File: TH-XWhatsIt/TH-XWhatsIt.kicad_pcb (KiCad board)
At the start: 2 copper layers, 178 x 115.5 mm, 41 parts, among them J1 COLUMNS, J10 DISPLAYWRITER PLUGBOARD CONNE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, J11 DISPLAYWRITER PLUGBOARD ROWS, J12 EXPANSION HEADER, J2 ROWS, J3 MODEL F PLUGBOARD COLUMNS, J4 MODEL F PLUGBOARD CONNECTOR, J5 MODEL F PLUGBOARD ROWS, J6 BEAMSPRING PLUGBOARD COLUMNS, J7 BEAMSPRING PLUGBOARD CONNECTOR, J8 BEAMSPRING PLUGBOARD ROWS, J9 DISPLAYWRITER PLUGBOARD COLUM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, U1 LM339, U2 MCP4921-EP, U3 74HCT595, U5 74HCT595, U6 LM339, U7 ProMicro, U8 74HCT595

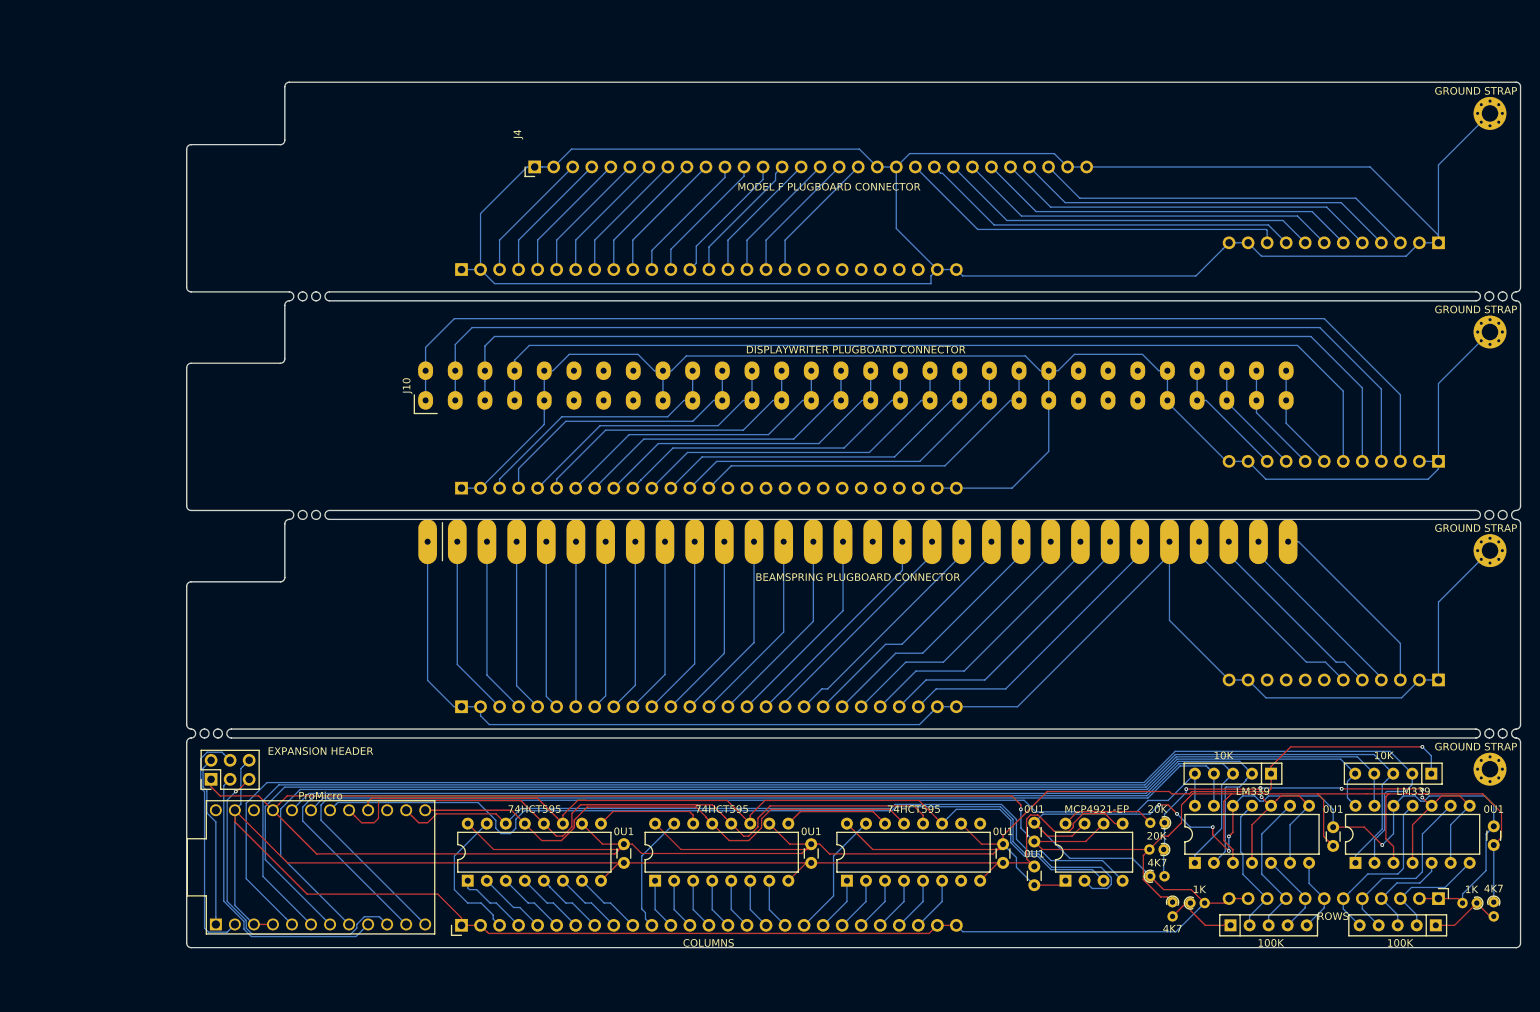
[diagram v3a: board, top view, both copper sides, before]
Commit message: initial update to switch to smd, so now th prefix is a misnomer
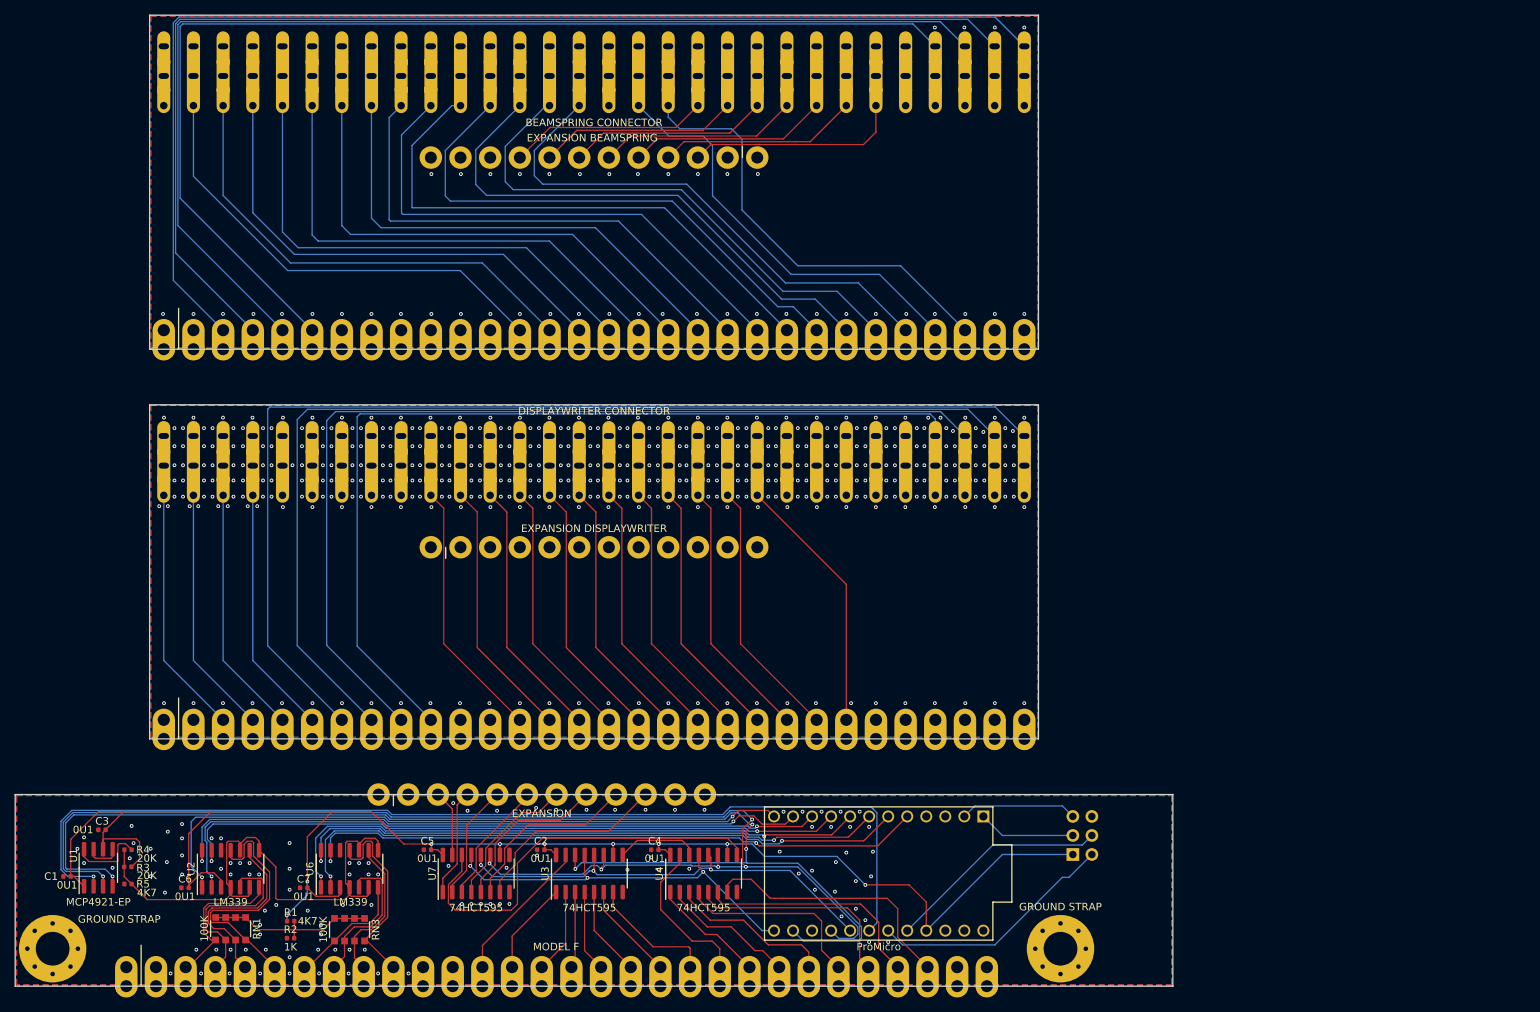
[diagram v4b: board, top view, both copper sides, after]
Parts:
- removed C10, C8, C9: 0U1, Capacitor_THT:C_Disc_D3.0mm_W1.6mm_P2.50mm
- removed H3, H4: GROUND STRAP, MountingHole:MountingHole_2.2mm_M2_Pad_Via
- removed J10: DISPLAYWRITER PLUGBOARD CONNECTOR, TH-XWhatsIt:DIP-60_155_ELL
- removed J11: DISPLAYWRITER PLUGBOARD ROWS, Connector_PinSocket_2.54mm:PinSocket_1x12_P2.54mm_Vertical
- removed J12: EXPANSION HEADER, Connector_PinHeader_2.54mm:PinHeader_2x03_P2.54mm_Vertical
- removed R6: 4K7, Resistor_THT:R_Axial_DIN0204_L3.6mm_D1.6mm_P1.90mm_Vertical
- removed R7: 1K, Resistor_THT:R_Axial_DIN0204_L3.6mm_D1.6mm_P1.90mm_Vertical
- removed RN2, RN4: 10K, Resistor_THT:R_Array_SIP5
- removed U8: 74HCT595, Package_DIP:DIP-16_W7.62mm
- added C1: 0U1, Capacitor_SMD:C_0402_1005Metric, F.Cu at (37.6, 139.3)
- added C2: 0U1, Capacitor_SMD:C_0402_1005Metric, F.Cu at (100.8, 135.8)
- added C6: 0U1, Capacitor_SMD:C_0402_1005Metric, F.Cu at (53.4, 140.8)
- added U4: 74HCT595, Package_SO:SOIC-16_3.9x9.9mm_P1.27mm, F.Cu at (122.6, 138.9)
- C3, C4, C5, C7: footprint Capacitor_THT:C_Disc_D3.0mm_W1.6mm_P2.50mm -> Capacitor_SMD:C_0402_1005Metric
- H1, H2: footprint MountingHole:MountingHole_2.2mm_M2_Pad_Via -> MountingHole:MountingHole_4.5mm_Pad_Via
- J1: value COLUMNS -> MODEL F; footprint Connector_PinHeader_2.54mm:PinHeader_1x27_P2.54mm_Vertical -> TH-XWhatsIt:30-pin-castelated-connector
- J2: value ROWS -> EXPANSION; footprint Connector_PinHeader_2.54mm:PinHeader_1x12_P2.54mm_Vertical -> TH-XWhatsIt:12-pin-castelated-connector
- J3: value MODEL F PLUGBOARD COLUMNS -> EXPANSION HEADER; footprint Connector_PinSocket_2.54mm:PinSocket_1x27_P2.54mm_Vertical -> Connector_PinHeader_2.54mm:PinHeader_2x03_P2.54mm_Horizontal
- J4: value MODEL F PLUGBOARD CONNECTOR -> EXPANSION BEAMSPRING; footprint Connector_PinHeader_2.54mm:PinHeader_1x30_P2.54mm_Horizontal -> TH-XWhatsIt:30-pin-castelated-connector
- J5: value MODEL F PLUGBOARD ROWS -> BEAMSPRING CONNECTOR; footprint Connector_PinSocket_2.54mm:PinSocket_1x12_P2.54mm_Vertical -> TH-XWhatsIt:30-pin-universal-beamspring-connector; moved to F.Cu
- J6: value BEAMSPRING PLUGBOARD COLUMNS -> EXPANSION BEAMSPRING; footprint Connector_PinSocket_2.54mm:PinSocket_1x27_P2.54mm_Vertical -> TH-XWhatsIt:12-pin-castelated-connector; moved to F.Cu
- J7: value BEAMSPRING PLUGBOARD CONNECTOR -> EXPANSION DISPLAYWRITER; footprint TH-XWhatsIt:3..6mm_cardedge -> TH-XWhatsIt:30-pin-castelated-connector
- J8: value BEAMSPRING PLUGBOARD ROWS -> DISPLAYWRITER CONNECTOR; footprint Connector_PinSocket_2.54mm:PinSocket_1x12_P2.54mm_Vertical -> TH-XWhatsIt:30-pin-universal-beamspring-connector; moved to F.Cu
- J9: value DISPLAYWRITER PLUGBOARD COLUMNS -> EXPANSION DISPLAYWRITER; footprint Connector_PinSocket_2.54mm:PinSocket_1x27_P2.54mm_Vertical -> TH-XWhatsIt:12-pin-castelated-connector; moved to F.Cu
- R1, R2, R3, R4, R5: footprint Resistor_THT:R_Axial_DIN0204_L3.6mm_D1.6mm_P1.90mm_Vertical -> Resistor_SMD:R_0402_1005Metric
- RN1, RN3: footprint Resistor_THT:R_Array_SIP5 -> Resistor_SMD:R_Array_Convex_4x1206
- U1: value LM339 -> MCP4921-EP; footprint Package_DIP:DIP-14_W7.62mm -> Package_SO:SOIC-8_3.9x4.9mm_P1.27mm
- U2: value MCP4921-EP -> LM339; footprint Package_DIP:DIP-8_W7.62mm -> Package_SO:SOIC-14_3.9x8.7mm_P1.27mm
- U3: footprint Package_DIP:DIP-16_W7.62mm -> Package_SO:SOIC-16_3.9x9.9mm_P1.27mm
- U5: value 74HCT595 -> ProMicro; footprint Package_DIP:DIP-16_W7.62mm -> promicro:ProMicro
- U6: footprint Package_DIP:DIP-14_W7.62mm -> Package_SO:SOIC-14_3.9x8.7mm_P1.27mm
- U7: value ProMicro -> 74HCT595; footprint promicro:ProMicro -> Package_SO:SOIC-16_3.9x9.9mm_P1.27mm
- moved H1 193.3 mm to (35.7, 149.0)
- moved U1 167.8 mm to (41.8, 138.2)
- moved RN1 160.8 mm to (59.4, 146.3), turned to 270 degrees
- moved R1 160.6 mm to (67.5, 145.3), turned to 0 degrees
- moved R2 158.4 mm to (67.4, 147.6), turned to 0 degrees
- moved R4 138.4 mm to (45.7, 135.8), turned to 0 degrees
- moved R3 138.3 mm to (45.7, 138.0), turned to 0 degrees
- moved R5 136.4 mm to (45.7, 140.3)
- moved H2 125.3 mm to (170.2, 149.0)
- moved C3 124.5 mm to (42.3, 133.1), turned to 0 degrees
- moved J2 120.5 mm to (101.0, 128.4), turned to 0 degrees
- moved RN3 117.6 mm to (75.3, 146.4), turned to 270 degrees
- moved J8 115.8 mm to (107.9, 86.5), turned to 0 degrees
- moved J5 114.5 mm to (107.9, 34.5), turned to 0 degrees
- moved J3 112.9 mm to (171.8, 136.4), turned to 0 degrees
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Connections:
- H2 pad 1: /model f plugboard/MFGROUND -> GNDA
- J1 pad 10: COL8 -> SENSE8
- J1 pad 11: COL9 -> GNDA
- J1 pad 12: COL10 -> GNDA
- J1 pad 13: COL11 -> COL1
- J1 pad 14: COL12 -> COL2
- J1 pad 15: COL13 -> COL3
- J1 pad 16: COL14 -> COL4
- J1 pad 17: COL15 -> COL5
- J1 pad 18: COL16 -> COL6
- J1 pad 19: COL17 -> COL7
- J1 pad 20: COL18 -> COL8
- J1 pad 21: COL19 -> COL9
- J1 pad 22: COL20 -> COL10
- J1 pad 23: COL21 -> COL11
- J1 pad 24: COL22 -> COL12
- J1 pad 25: COL23 -> COL13
- J1 pad 26: GNDA -> COL14
- J1 pad 27: GNDA -> COL15
- J1 pad 3: COL1 -> SENSE1
- J1 pad 4: COL2 -> SENSE2
- J1 pad 5: COL3 -> SENSE3
- J1 pad 6: COL4 -> SENSE4
- J1 pad 7: COL5 -> SENSE5
- J1 pad 8: COL6 -> SENSE7
- J1 pad 9: COL7 -> SENSE6
- J2 pad 10: SENSE8 -> COL24
- J2 pad 3: SENSE1 -> COL17
- J2 pad 4: SENSE2 -> COL18
- J2 pad 5: SENSE3 -> COL19
- J2 pad 6: SENSE4 -> COL20
- J2 pad 7: SENSE5 -> COL21
- J2 pad 8: SENSE7 -> COL22
- J2 pad 9: SENSE6 -> COL23
- J3 pad 1: /model f plugboard/MFGROUND -> +5VA
- J3 pad 2: /model f plugboard/MFGROUND -> HEADER3
- J3 pad 3: /model f plugboard/MFCOL1 -> HEADER1
- J3 pad 4: /model f plugboard/MFCOL2 -> HEADER4
- J3 pad 5: /model f plugboard/MFCOL3 -> HEADER2
- J3 pad 6: /model f plugboard/MFCOL4 -> GNDA
- J4 pad 1: /model f plugboard/MFGROUND -> /beamspring plugboard/BSGROUND
- J4 pad 10: /model f plugboard/MFCOL8 -> Net-(J4-Pad10)
- J4 pad 11: /model f plugboard/MFCOL9 -> /beamspring plugboard/BSGROUND
- J4 pad 12: /model f plugboard/MFCOL10 -> /beamspring plugboard/BSGROUND
- J4 pad 13: /model f plugboard/MFCOL11 -> /beamspring plugboard/BSCOL1
- J4 pad 14: /model f plugboard/MFCOL12 -> /beamspring plugboard/BSCOL2
- J4 pad 15: /model f plugboard/MFCOL13 -> /beamspring plugboard/BSCOL3
- J4 pad 16: /model f plugboard/MFCOL14 -> /beamspring plugboard/BSCOL4
- J4 pad 17: /model f plugboard/MFCOL15 -> /beamspring plugboard/BSCOL5
- J4 pad 18: /model f plugboard/MFCOL16 -> /beamspring plugboard/BSCOL6
- J4 pad 19: /model f plugboard/MFGROUND -> /beamspring plugboard/BSCOL7
- J4 pad 2: /model f plugboard/MFGROUND -> /beamspring plugboard/BSGROUND
- J4 pad 20: /model f plugboard/MFGROUND -> /beamspring plugboard/BSCOL8
- J4 pad 21: /model f plugboard/MFSENSE1 -> /beamspring plugboard/BSCOL9
- J4 pad 22: /model f plugboard/MFSENSE2 -> /beamspring plugboard/BSCOL10
- J4 pad 23: /model f plugboard/MFSENSE3 -> /beamspring plugboard/BSCOL11
- J4 pad 24: /model f plugboard/MFSENSE4 -> /beamspring plugboard/BSCOL12
- J4 pad 25: /model f plugboard/MFSENSE5 -> /beamspring plugboard/BSCOL13
- J4 pad 26: /model f plugboard/MFSENSE6 -> /beamspring plugboard/BSCOL14
- J4 pad 27: /model f plugboard/MFSENSE7 -> /beamspring plugboard/BSCOL15
- J4 pad 28: /model f plugboard/MFSENSE8 -> /beamspring plugboard/BSCOL16
- J4 pad 29: /model f plugboard/MFGROUND -> /beamspring plugboard/BSGROUND
- J4 pad 3: /model f plugboard/MFCOL1 -> /beamspring plugboard/BSSENSE4
- J4 pad 30: /model f plugboard/MFGROUND -> /beamspring plugboard/BSGROUND
- J4 pad 4: /model f plugboard/MFCOL2 -> /beamspring plugboard/BSSENSE3
- J4 pad 5: /model f plugboard/MFCOL3 -> /beamspring plugboard/BSSENSE2
- J4 pad 6: /model f plugboard/MFCOL4 -> /beamspring plugboard/BSSENSE1
- J4 pad 7: /model f plugboard/MFCOL5 -> Net-(J4-Pad7)
- J4 pad 8: /model f plugboard/MFCOL6 -> Net-(J4-Pad8)
- J4 pad 9: /model f plugboard/MFCOL7 -> Net-(J4-Pad9)
- J5 pad 1: /model f plugboard/MFGROUND -> /beamspring plugboard/BSGROUND
- J5 pad 10: /model f plugboard/MFSENSE1 -> /beamspring plugboard/BSCOL9
- J5 pad 11: /model f plugboard/MFGROUND -> /beamspring plugboard/BSCOL10
- J5 pad 12: /model f plugboard/MFGROUND -> /beamspring plugboard/BSCOL11
- J5 pad 2: /model f plugboard/MFGROUND -> /beamspring plugboard/BSCOL1
- J5 pad 3: /model f plugboard/MFSENSE8 -> /beamspring plugboard/BSCOL2
- J5 pad 4: /model f plugboard/MFSENSE7 -> /beamspring plugboard/BSCOL3
- J5 pad 5: /model f plugboard/MFSENSE6 -> /beamspring plugboard/BSCOL4
- J5 pad 6: /model f plugboard/MFSENSE5 -> /beamspring plugboard/BSCOL5
- J5 pad 7: /model f plugboard/MFSENSE4 -> /beamspring plugboard/BSCOL6
- J5 pad 8: /model f plugboard/MFSENSE3 -> /beamspring plugboard/BSCOL7
- J5 pad 9: /model f plugboard/MFSENSE2 -> /beamspring plugboard/BSCOL8
- J6 pad 10: /beamspring plugboard/BSCOL8 -> (no net)
- J6 pad 11: /beamspring plugboard/BSCOL9 -> /beamspring plugboard/BSGROUND
- J6 pad 12: /beamspring plugboard/BSCOL10 -> /beamspring plugboard/BSGROUND
- J6 pad 3: /beamspring plugboard/BSCOL1 -> /beamspring plugboard/BSCOL23
- J6 pad 4: /beamspring plugboard/BSCOL2 -> /beamspring plugboard/BSCOL22
- J6 pad 5: /beamspring plugboard/BSCOL3 -> /beamspring plugboard/BSCOL21
- J6 pad 6: /beamspring plugboard/BSCOL4 -> /beamspring plugboard/BSCOL20
- J6 pad 7: /beamspring plugboard/BSCOL5 -> /beamspring plugboard/BSCOL19
- J6 pad 8: /beamspring plugboard/BSCOL6 -> /beamspring plugboard/BSCOL18
- J6 pad 9: /beamspring plugboard/BSCOL7 -> /beamspring plugboard/BSCOL17
- J7 pad 1: /beamspring plugboard/BSGROUND -> /displaywriter plugboard/DWGROUND
- J7 pad 10: /beamspring plugboard/BSCOL9 -> /displaywriter plugboard/DWSENSE8
- J7 pad 11: /beamspring plugboard/BSCOL10 -> /displaywriter plugboard/DWGROUND
- J7 pad 12: /beamspring plugboard/BSCOL11 -> /displaywriter plugboard/DWGROUND
- J7 pad 13: /beamspring plugboard/BSCOL12 -> /displaywriter plugboard/DWCOL1
- J7 pad 14: /beamspring plugboard/BSCOL13 -> /displaywriter plugboard/DWCOL2
- J7 pad 15: /beamspring plugboard/BSCOL14 -> /displaywriter plugboard/DWCOL3
- J7 pad 16: (no net) -> /displaywriter plugboard/DWCOL4
- J7 pad 17: /beamspring plugboard/BSCOL15 -> /displaywriter plugboard/DWCOL5
- J7 pad 18: /beamspring plugboard/BSCOL16 -> /displaywriter plugboard/DWCOL6
- J7 pad 19: /beamspring plugboard/BSCOL17 -> /displaywriter plugboard/DWCOL7
- J7 pad 2: /beamspring plugboard/BSCOL1 -> /displaywriter plugboard/DWGROUND
- J7 pad 20: /beamspring plugboard/BSCOL18 -> /displaywriter plugboard/DWCOL8
- J7 pad 21: /beamspring plugboard/BSCOL19 -> /displaywriter plugboard/DWCOL9
- J7 pad 22: /beamspring plugboard/BSCOL20 -> /displaywriter plugboard/DWCOL10
- J7 pad 23: /beamspring plugboard/BSCOL21 -> /displaywriter plugboard/DWCOL11
- J7 pad 24: /beamspring plugboard/BSCOL22 -> /displaywriter plugboard/DWCOL12
- J7 pad 25: /beamspring plugboard/BSCOL23 -> Net-(J7-Pad25)
- J7 pad 26: /beamspring plugboard/BSGROUND -> Net-(J7-Pad26)
- J7 pad 27: /beamspring plugboard/BSSENSE1 -> Net-(J7-Pad27)
- J7 pad 28: /beamspring plugboard/BSSENSE2 -> Net-(J7-Pad28)
- J7 pad 29: /beamspring plugboard/BSSENSE3 -> /displaywriter plugboard/DWGROUND
- J7 pad 3: /beamspring plugboard/BSCOL2 -> /displaywriter plugboard/DWSENSE1
- J7 pad 30: /beamspring plugboard/BSSENSE4 -> /displaywriter plugboard/DWGROUND
- J7 pad 4: /beamspring plugboard/BSCOL3 -> /displaywriter plugboard/DWSENSE2
- J7 pad 5: /beamspring plugboard/BSCOL4 -> /displaywriter plugboard/DWSENSE3
- J7 pad 6: /beamspring plugboard/BSCOL5 -> /displaywriter plugboard/DWSENSE4
- J7 pad 7: /beamspring plugboard/BSCOL6 -> /displaywriter plugboard/DWSENSE5
- J7 pad 8: /beamspring plugboard/BSCOL7 -> /displaywriter plugboard/DWSENSE6
- J7 pad 9: /beamspring plugboard/BSCOL8 -> /displaywriter plugboard/DWSENSE7
- J8 pad 1: /beamspring plugboard/BSGROUND -> /displaywriter plugboard/DWSENSE1
- J8 pad 10: (no net) -> /displaywriter plugboard/DWCOL1
- J8 pad 11: /beamspring plugboard/BSGROUND -> /displaywriter plugboard/DWCOL2
- J8 pad 12: /beamspring plugboard/BSGROUND -> /displaywriter plugboard/DWCOL3
- J8 pad 2: /beamspring plugboard/BSGROUND -> /displaywriter plugboard/DWSENSE2
- J8 pad 3: /beamspring plugboard/BSSENSE4 -> /displaywriter plugboard/DWSENSE3
- J8 pad 4: /beamspring plugboard/BSSENSE3 -> /displaywriter plugboard/DWSENSE4
- J8 pad 5: /beamspring plugboard/BSSENSE2 -> /displaywriter plugboard/DWGROUND
- J8 pad 6: /beamspring plugboard/BSSENSE1 -> Net-(J8-Pad6)
- J8 pad 7: (no net) -> Net-(J8-Pad7)
- J8 pad 8: (no net) -> Net-(J8-Pad8)
- J8 pad 9: (no net) -> /displaywriter plugboard/DWGROUND
- J9 pad 10: /displaywriter plugboard/DWCOL8 -> (no net)
- J9 pad 11: /displaywriter plugboard/DWCOL9 -> /displaywriter plugboard/DWGROUND
- J9 pad 12: /displaywriter plugboard/DWCOL10 -> /displaywriter plugboard/DWGROUND
- J9 pad 3: /displaywriter plugboard/DWCOL1 -> (no net)
- J9 pad 4: /displaywriter plugboard/DWCOL2 -> (no net)
- J9 pad 5: /displaywriter plugboard/DWCOL3 -> (no net)
- J9 pad 6: /displaywriter plugboard/DWCOL4 -> (no net)
- J9 pad 7: /displaywriter plugboard/DWCOL5 -> (no net)
- J9 pad 8: /displaywriter plugboard/DWCOL6 -> (no net)
- J9 pad 9: /displaywriter plugboard/DWCOL7 -> (no net)
- R1 pad 2: Net-(R1-Pad2) -> BIAS
- R2 pad 1: Net-(R1-Pad2) -> GNDA
- R2 pad 2: GNDA -> BIAS
- RN1 pad 1: Net-(R1-Pad2) -> BIAS
- RN1 pad 2: SENSE1 -> BIAS
- RN1 pad 3: SENSE2 -> BIAS
- RN1 pad 4: SENSE3 -> BIAS
- RN1 pad 5: SENSE4 -> SENSE1
- RN3 pad 1: Net-(R6-Pad2) -> BIAS
- RN3 pad 2: SENSE8 -> BIAS
- RN3 pad 3: SENSE6 -> BIAS
- RN3 pad 4: SENSE7 -> BIAS
- U1 pad 1: ROW1 -> +5VA
- U1 pad 2: ROW2 -> ~SELECTDAC
- U1 pad 3: +5VA -> CLOCK
- U1 pad 4: SETPOINT -> MOSI
- U1 pad 5: SENSE2 -> GNDA
- U1 pad 6: SETPOINT -> +5VA
- U1 pad 7: SENSE1 -> GNDA
- U1 pad 8: SETPOINT -> Net-(R4-Pad2)
- U2 pad 1: +5VA -> ROW1
- U2 pad 2: ~SELECTDAC -> ROW2
- U2 pad 3: CLOCK -> +5VA
- U2 pad 4: MOSI -> SETPOINT
- U2 pad 5: GNDA -> SENSE2
- U2 pad 6: +5VA -> SETPOINT
- U2 pad 7: GNDA -> SENSE1
- U2 pad 8: Net-(R4-Pad2) -> SETPOINT
- U5 pad 1: COL10 -> HEADER1
- U5 pad 10: +5VA -> ROW2
- U5 pad 11: CLOCK -> ROW3
- U5 pad 12: LOADCOL -> ROW1
- U5 pad 14: SERIALOUT1 -> MOSI
- U5 pad 15: COL9 -> GNDA
- U5 pad 16: +5VA -> CLOCK
- U5 pad 2: COL11 -> HEADER2
- U5 pad 3: COL12 -> GNDA
- U5 pad 4: COL13 -> GNDA
- U5 pad 5: COL14 -> ROW8
- U5 pad 6: COL15 -> ROW7
- U5 pad 7: COL16 -> ROW6
- U5 pad 8: GNDA -> ROW5
- U5 pad 9: SERIALOUT2 -> ROW4
- U7 pad 1: HEADER3 -> COL18
- U7 pad 10: HEADER2 -> +5VA
- U7 pad 11: ROW5 -> CLOCK
- U7 pad 12: ROW6 -> LOADCOL
- U7 pad 14: MOSI -> SERIALOUT2
- U7 pad 15: (no net) -> COL17
- U7 pad 16: CLOCK -> +5VA
- U7 pad 2: HEADER4 -> COL19
- U7 pad 3: GNDA -> COL20
- U7 pad 4: GNDA -> COL21
- U7 pad 5: ROW2 -> COL22
- U7 pad 6: ROW1 -> COL23
- U7 pad 7: ROW4 -> COL24
- U7 pad 8: ROW3 -> GNDA
- U7 pad 9: HEADER1 -> (no net)
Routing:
- net GNDA: track 455.3 -> 4.68 mm, vias 6 -> 109
- net /model f plugboard/MFGROUND: track 318.4 -> 0.00 mm
- net +5VA: track 516.9 -> 226.1 mm, vias 2 -> 9
- net /displaywriter plugboard/DWGROUND: track 210.6 -> 15.8 mm, vias 0 -> 381
- net /beamspring plugboard/BSGROUND: track 203.6 -> 15.8 mm, vias 0 -> 46
- net /beamspring plugboard/BSSENSE4: track 25.5 -> 167.2 mm
- net /displaywriter plugboard/DWSENSE5: track 16.7 -> 156.3 mm
- net /beamspring plugboard/BSSENSE3: track 25.2 -> 164.1 mm
- net /beamspring plugboard/BSSENSE2: track 26.5 -> 161.0 mm
- net /displaywriter plugboard/DWSENSE6: track 15.4 -> 147.2 mm
- net /beamspring plugboard/BSSENSE1: track 27.9 -> 157.9 mm
- net /displaywriter plugboard/DWSENSE7: track 14.8 -> 139.9 mm
- net /displaywriter plugboard/DWSENSE8: track 14.2 -> 132.3 mm
- net /displaywriter plugboard/DWSENSE1: track 151.8 -> 41.2 mm
- net /displaywriter plugboard/DWSENSE2: track 145.0 -> 41.2 mm
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- added copper zone on B.Cu, net /beamspring plugboard/BSGROUND
- added copper zone on F.Cu, net /beamspring plugboard/BSGROUND
- added copper zone on B.Cu, net /displaywriter plugboard/DWGROUND
- added copper zone on F.Cu, net /displaywriter plugboard/DWGROUND
- added copper zone on B.Cu, net GNDA
- added copper zone on F.Cu, net GNDA
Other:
- board size 178 x 115.5 mm -> 154.5 x 129.6 mm

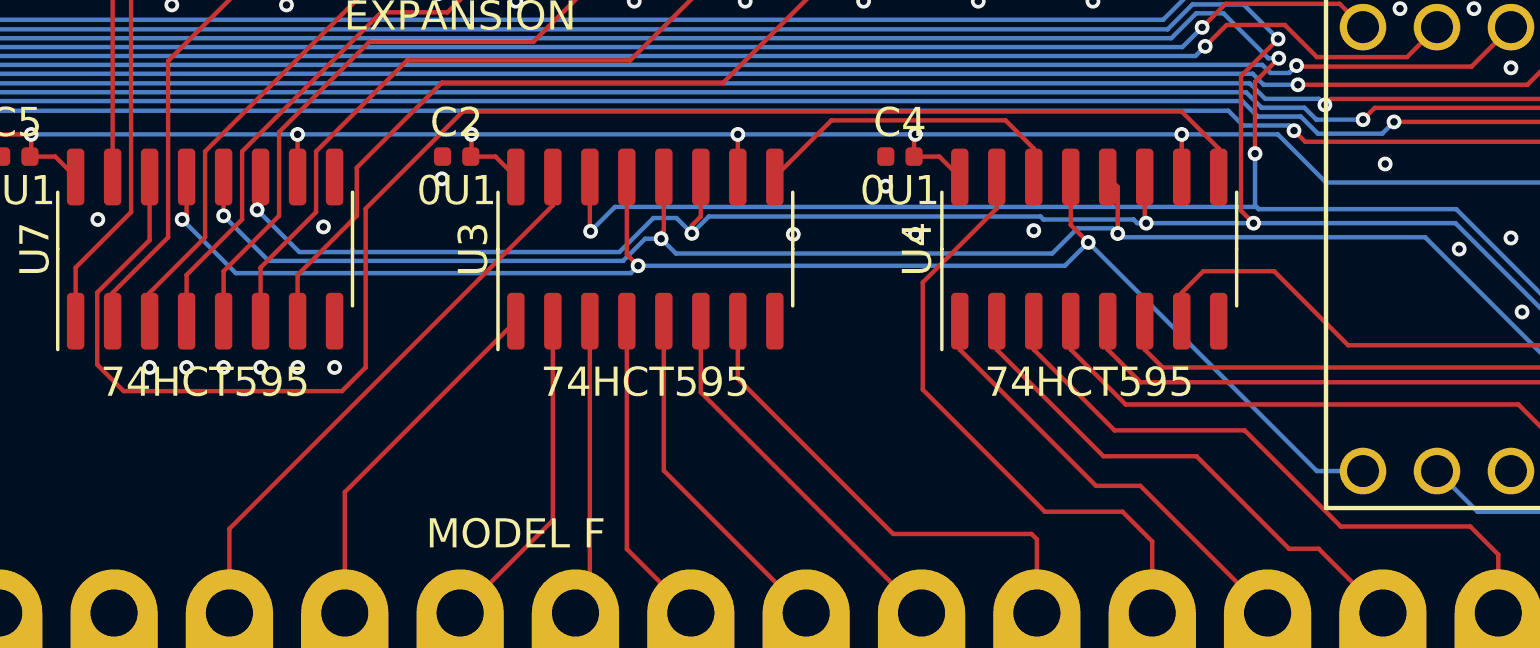
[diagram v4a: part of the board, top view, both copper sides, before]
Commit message: pcb: pushed update from schematic: (OE grounded)
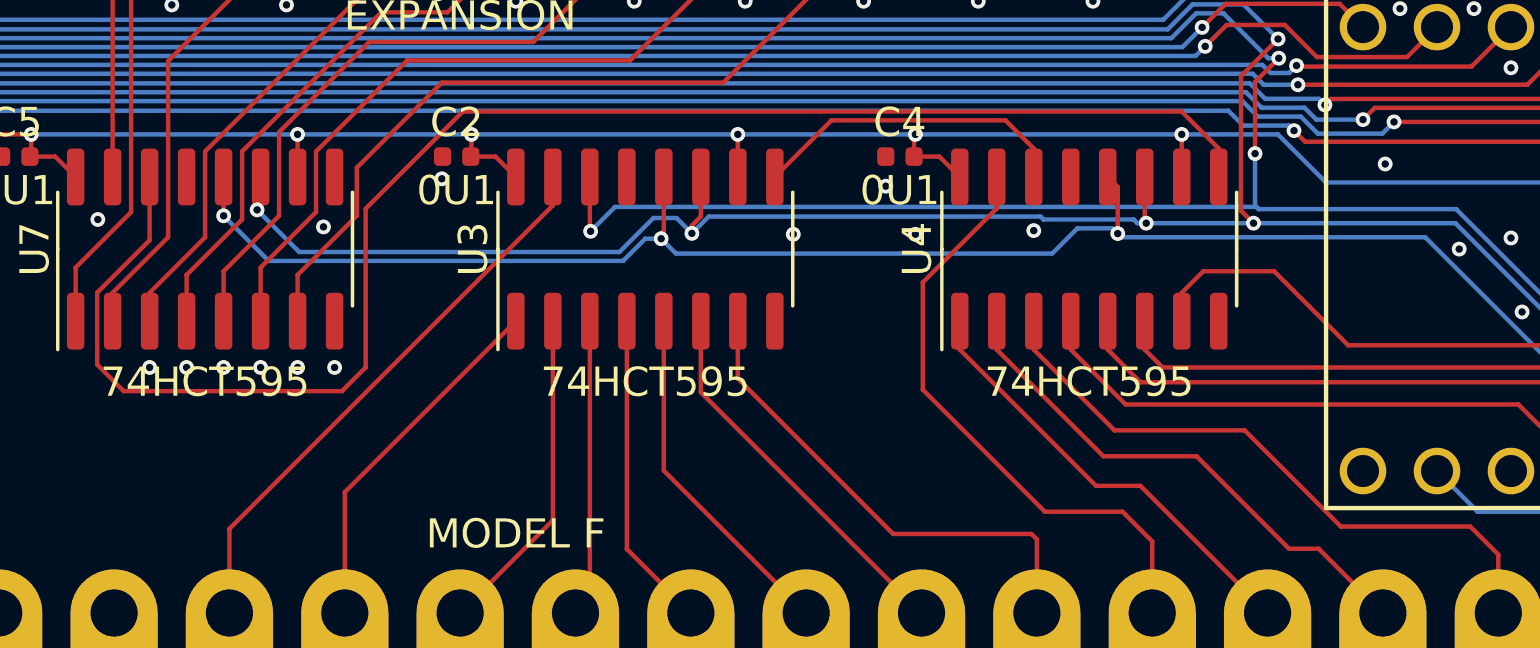
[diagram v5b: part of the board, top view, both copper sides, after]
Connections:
- J6 pad 10: (no net) -> Net-(J6-Pad10)
- J9 pad 10: (no net) -> Net-(J9-Pad10)
- J9 pad 3: (no net) -> Net-(J9-Pad3)
- J9 pad 4: (no net) -> Net-(J9-Pad4)
- J9 pad 5: (no net) -> Net-(J9-Pad5)
- J9 pad 6: (no net) -> Net-(J9-Pad6)
- J9 pad 7: (no net) -> Net-(J9-Pad7)
- J9 pad 8: (no net) -> Net-(J9-Pad8)
- J9 pad 9: (no net) -> Net-(J9-Pad9)
- U3 pad 13: ~OE -> GNDA
- U4 pad 13: ~OE -> GNDA
- U5 pad 13: ~OE -> GNDA
- U5 pad 22: (no net) -> Net-(U5-Pad22)
- U5 pad 24: (no net) -> Net-(U5-Pad24)
- U7 pad 13: ~OE -> GNDA
- U7 pad 9: (no net) -> Net-(U7-Pad9)
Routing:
- net ~OE: track 52.2 -> 0.00 mm, vias 3 -> 0

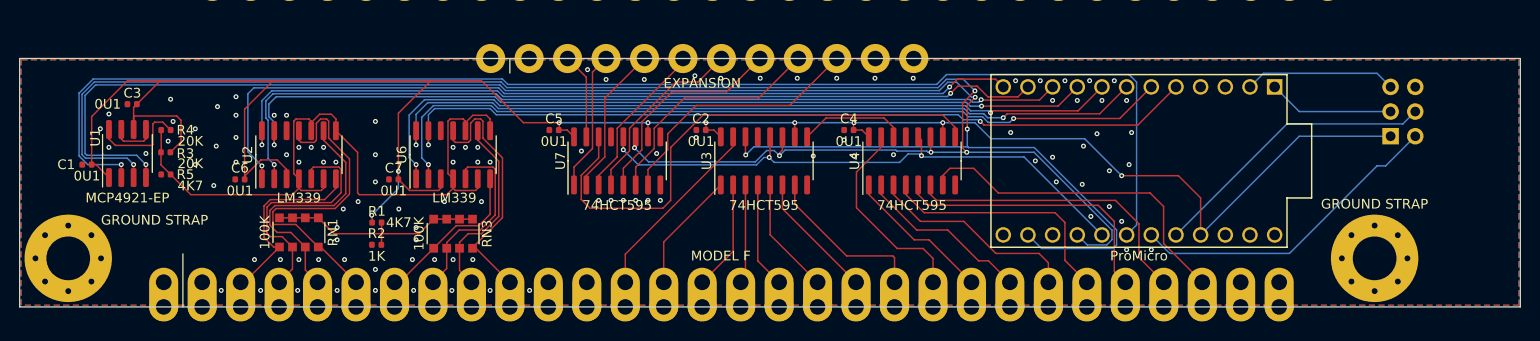
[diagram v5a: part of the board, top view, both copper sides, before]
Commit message: pcb: made solenoid header footprint vertical, removed right side of controller PCB
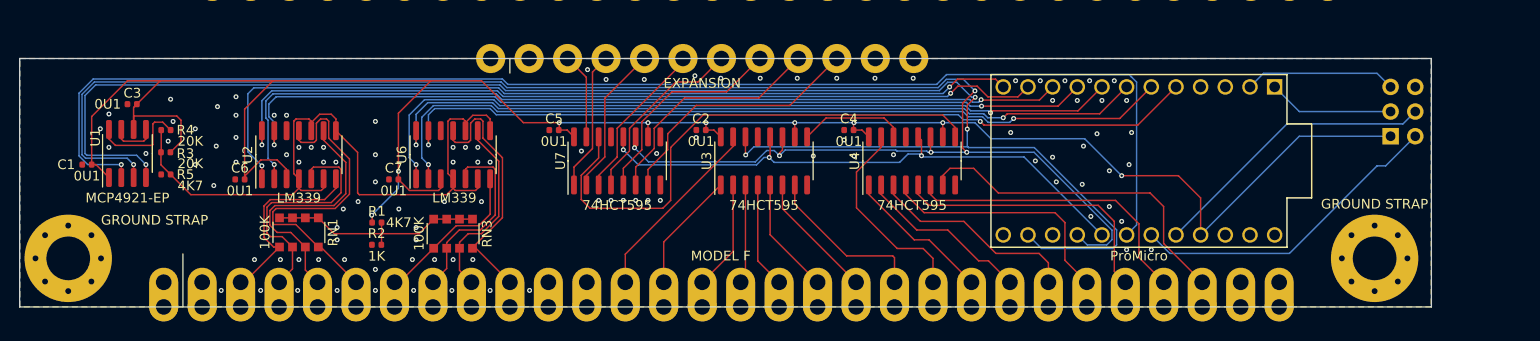
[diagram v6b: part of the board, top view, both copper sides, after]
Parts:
- J3: footprint Connector_PinHeader_2.54mm:PinHeader_2x03_P2.54mm_Horizontal -> Connector_PinHeader_2.54mm:PinHeader_2x03_P2.54mm_Vertical
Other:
- board size 154.5 x 129.6 mm -> 145.3 x 129.6 mm
